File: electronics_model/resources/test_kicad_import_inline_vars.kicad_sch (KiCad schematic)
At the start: 3 parts

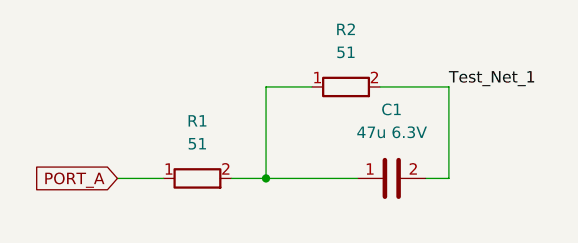
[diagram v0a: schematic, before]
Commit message: KiCad Schematic Import (#183)
Instead of importing netlists, this now directly imports schematics and
netlists from that. There are 3 methods:
- Block defined in HDL, connectivity loaded from KiCad using refdes.
- Block defined in KiCad using inline Python
- Block defined in KiCad, where the Block class defines symbol parsing
rules (eg, resistor with value "51" is parsed as a 51-ohm resistor +/- a
default tolerance of 5%)

Also adds a more general infrastructure to add KiCad value parsing rules
and symbol pin mapping rules to any block, through superclasses
KiCadInstantiableBlock (creates a Block model from a KiCad symbol) and
KiCadImportableBlock (defines symbol pinning) respectively.

Notes
- Infrastructure and unit tests only, no libraries or full examples use
this (yet).
- The netlist-from-schematic recognizes symbols, connected pins, and
labels on nets (including labels used as tunnels).
- The netlist-from-schematic isn't perfect, it doesn't detect
intersections.
- Adds parsing rules for resistors (resistance), capacitors
(capacitance, voltage), and opamps (no parameters).
- Refactors some utils in PartsTable (in electronics_abstract_parts) to
be used in the symbol parser (in the base package electronics_model)
- This replaces the kinparse (KiCad netlist parser) dependency with
sexpdata (s-expression parser). Bonus, it doesn't leave hanging open
files!
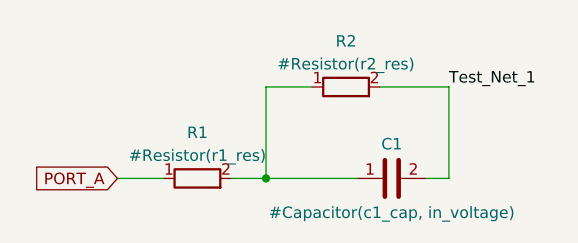
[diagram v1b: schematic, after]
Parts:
- C1: value 47u 6.3V -> #Capacitor(c1_cap, in_voltage)
- R1: value 51 -> #Resistor(r1_res)
- R2: value 51 -> #Resistor(r2_res)
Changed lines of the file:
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@@
   )
   (symbol (lib_name "R_1") (lib_id "Device:R") (at 100.33 86.36 90) (unit 1)
-    (in_bom yes) (on_board yes) (fields_autoplaced)
-    (property "Reference" "R2" (id 0) (at 100.33 80.01 90))
-    (property "Value" "51" (id 1) (at 100.33 82.55 90))
+    (in_bom yes) (on_board yes)
+    (property "Reference" "R2" (id 0) (at 100.33 81.28 90))
+    (property "Value" "#Resistor(r2_res)" (id 1) (at 100.33 83.82 90))
     (property "Footprint" "" (id 2) (at 100.33 88.138 90)
       (effects (font (size 1.27 1.27)) hide)
@@
   )
   (symbol (lib_id "Device:R") (at 83.82 96.52 90) (unit 1)
-    (in_bom yes) (on_board yes) (fields_autoplaced)
-    (property "Reference" "R1" (id 0) (at 83.82 90.17 90))
-    (property "Value" "51" (id 1) (at 83.82 92.71 90))
+    (in_bom yes) (on_board yes)
+    (property "Reference" "R1" (id 0) (at 83.82 91.44 90))
+    (property "Value" "#Resistor(r1_res)" (id 1) (at 83.82 93.98 90))
     (property "Footprint" "" (id 2) (at 83.82 98.298 90)
       (effects (font (size 1.27 1.27)) hide)
@@
   )
   (symbol (lib_id "Device:C") (at 105.41 96.52 90) (unit 1)
-    (in_bom yes) (on_board yes) (fields_autoplaced)
-    (property "Reference" "C1" (id 0) (at 105.41 88.9 90))
-    (property "Value" "47u 6.3V" (id 1) (at 105.41 91.44 90))
+    (in_bom yes) (on_board yes)
+    (property "Reference" "C1" (id 0) (at 105.41 92.71 90))
+    (property "Value" "#Capacitor(c1_cap, in_voltage)" (id 1) (at 105.41 100.33 90))
     (property "Footprint" "" (id 2) (at 109.22 95.5548 0)
       (effects (font (size 1.27 1.27)) hide)
@@
   (symbol_instances
     (path "/e8ed392d-e797-4a51-a62e-0d0cb2854712"
-      (reference "C1") (unit 1) (value "47u 6.3V") (footprint "")
+      (reference "C1") (unit 1) (value "#Capacitor(c1_cap, in_voltage)") (footprint "")
     )
     (path "/691e9d02-a5cc-48a1-b9c1-b97da20de9cd"
-      (reference "R1") (unit 1) (value "51") (footprint "")
+      (reference "R1") (unit 1) (value "#Resistor(r1_res)") (footprint "")
     )
     (path "/053518b3-994e-4e57-8f86-80f07be5a072"
-      (reference "R2") (unit 1) (value "51") (footprint "")
+      (reference "R2") (unit 1) (value "#Resistor(r2_res)") (footprint "")
     )
   )

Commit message: Refactor examples / libraries to use import KiCad schematics (#184)
Refactors a lot of analog blocks (most opamp topologies, analog
switches) to be KiCad importable blocks (by defining a symbol pin
mapping) and/or KiCad imported schematics. Adds custom symbols for many
of these parts, some KiCad's base symbol library for the most part lacks
abstract / generic and high-level parts.

Netlists of example designs should not have changed.

KiCad import behavior change:
- global labels must connect to either a node or external block port and
are not treated as link names
- net labels are used as link names and must not collide with any
existing object member
- add unit tests for the above
- schematic now works on a fixed grid so points can be rounded to the
nearest point that lines up - it turns out points on schematic files can
be off by like 0.05 or something which broke the previous netlister
- support power nets (eg, GND, Vcc symbols)
- power nets and all labels are treated as connected in the schematic
importer (instead of punted up to the block to be handled as connected
in separate connect statements)
- support inline modified symbols (lib_name vs lib_id)
- support symbol mirror, fix rotation calculation (and unit test all of
this)
- import blocks in schematic in xy order (or optionally file order -
this isn't used)
- add a `file_path` utility function to KiCadSchematicBlock which
returns a relative path from the calling file
- moves some tests (mainly rotation, mirror, symbol connectivity) to be
schematic parser tests only, because it's a bit extra (and probably
doesn't tell us much more) to go all the way to Block proto

Infrastructural changes:
- refactors some existing symbol mappings to use pin names instead of
numbers
- refactors some existing symbol mappings to use Mapping return type
which is type covariant
- for connection type errors (link inference errors), prints the names
of the ports involved
- some better error 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
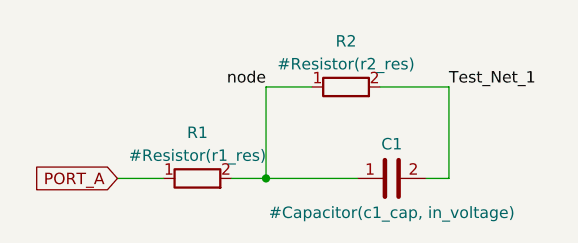
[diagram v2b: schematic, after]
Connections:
- net node: now reaches C1.1, R1.2, R2.1
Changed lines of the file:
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@@
     (stroke (width 0) (type default) (color 0 0 0 0))
+  )
+  (label "node" (at 91.44 86.36 180)
+    (effects (font (size 1.27 1.27)) (justify right bottom))
   )
   (label "Test_Net_1" (at 111.76 86.36 0)
@@
     )
   )
-  (symbol (lib_name "R_1") (lib_id "Device:R") (at 100.33 86.36 90) (unit 1)
-    (in_bom yes) (on_board yes)
-    (property "Reference" "R2" (id 0) (at 100.33 81.28 90))
-    (property "Value" "#Resistor(r2_res)" (id 1) (at 100.33 83.82 90))
-    (property "Footprint" "" (id 2) (at 100.33 88.138 90)
-      (effects (font (size 1.27 1.27)) hide)
-    )
-    (property "Datasheet" "~" (id 3) (at 100.33 86.36 0)
-      (effects (font (size 1.27 1.27)) hide)
-    )
-    (pin "1")
-    (pin "2")
-  )
   (symbol (lib_id "Device:R") (at 83.82 96.52 90) (unit 1)
     (in_bom yes) (on_board yes)
@@
     )
     (property "Datasheet" "~" (id 3) (at 83.82 96.52 0)
+      (effects (font (size 1.27 1.27)) hide)
+    )
+    (pin "1")
+    (pin "2")
+  )
+  (symbol (lib_id "Device:R") (at 100.33 86.36 90) (unit 1)
+    (in_bom yes) (on_board yes)
+    (property "Reference" "R2" (id 0) (at 100.33 81.28 90))
+    (property "Value" "#Resistor(r2_res)" (id 1) (at 100.33 83.82 90))
+    (property "Footprint" "" (id 2) (at 100.33 88.138 90)
+      (effects (font (size 1.27 1.27)) hide)
+    )
+    (property "Datasheet" "~" (id 3) (at 100.33 86.36 0)
       (effects (font (size 1.27 1.27)) hide)
     )
@@
       (reference "R1") (unit 1) (value "#Resistor(r1_res)") (footprint "")
     )
-    (path "/053518b3-994e-4e57-8f86-80f07be5a072"
+    (path "/baf72979-63e5-4a61-a0b3-2466221a7b9b"
       (reference "R2") (unit 1) (value "#Resistor(r2_res)") (footprint "")
     )

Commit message: unify naming
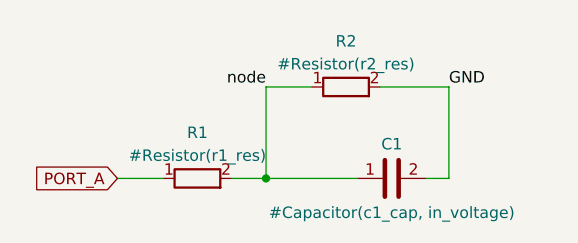
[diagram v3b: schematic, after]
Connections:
- net Test_Net_1 renamed GND
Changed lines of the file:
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@@
     (effects (font (size 1.27 1.27)) (justify right bottom))
   )
-  (label "Test_Net_1" (at 111.76 86.36 0)
+  (label "GND" (at 111.76 86.36 0)
     (effects (font (size 1.27 1.27)) (justify left bottom))
   )
